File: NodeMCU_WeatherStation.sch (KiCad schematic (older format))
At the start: 3 parts, among them J4 Conn_01x04, J5 Conn_01x04, U1 BME280

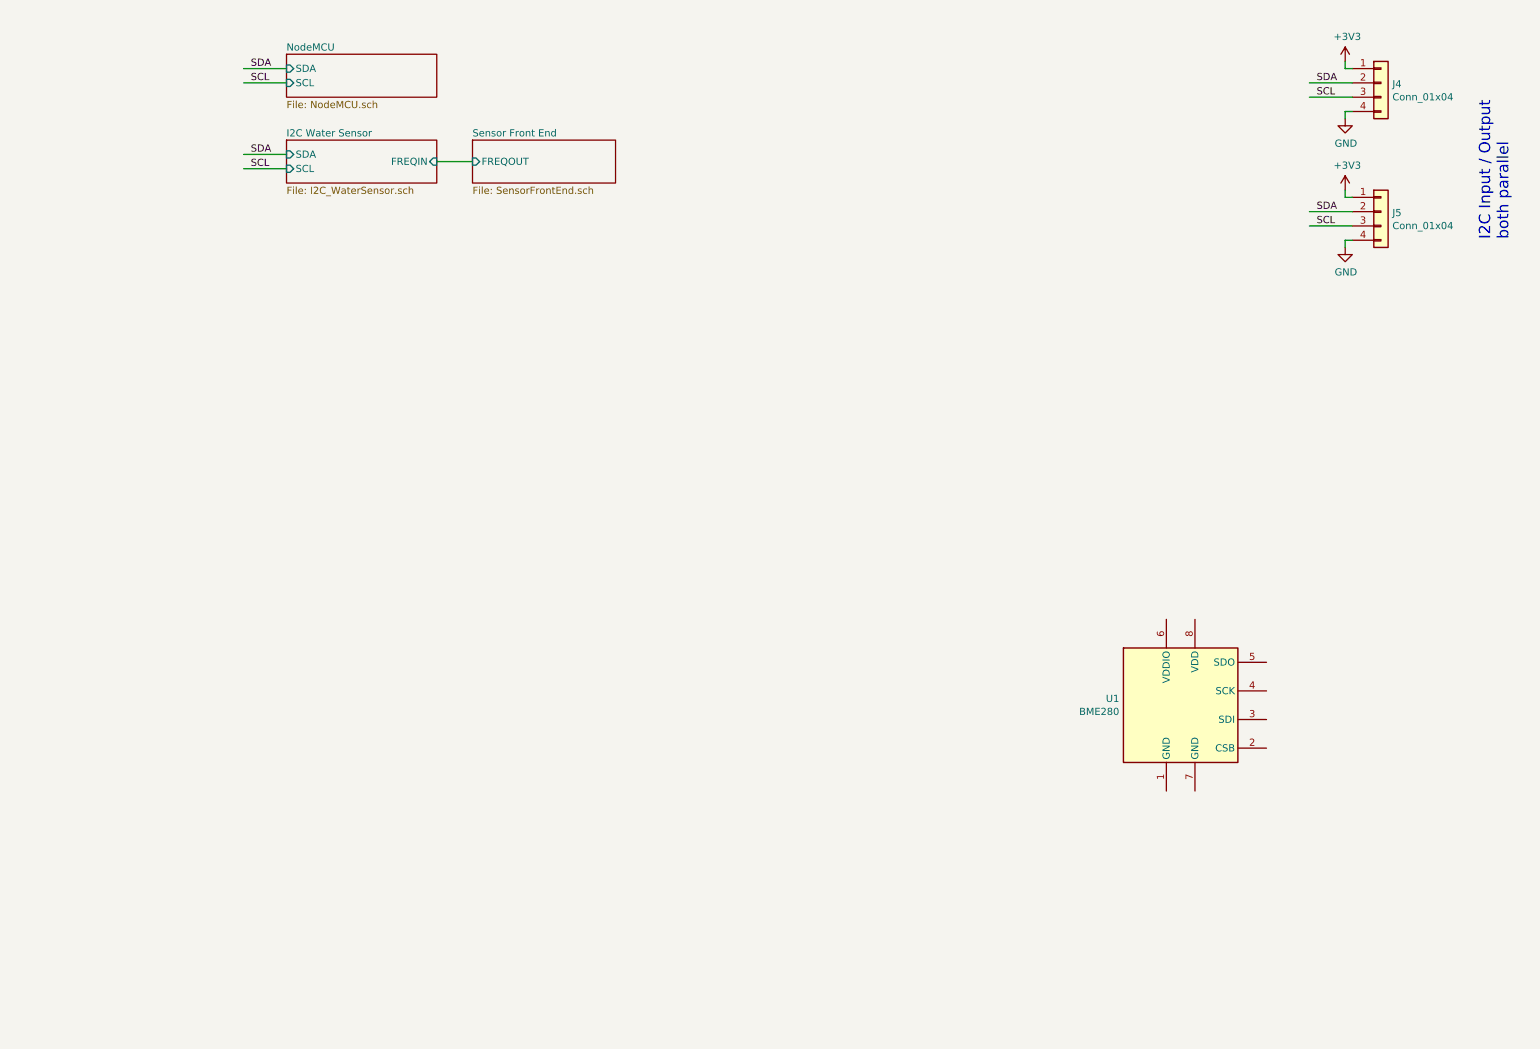
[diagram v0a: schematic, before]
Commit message: added 4-20mA input and PT100 readout
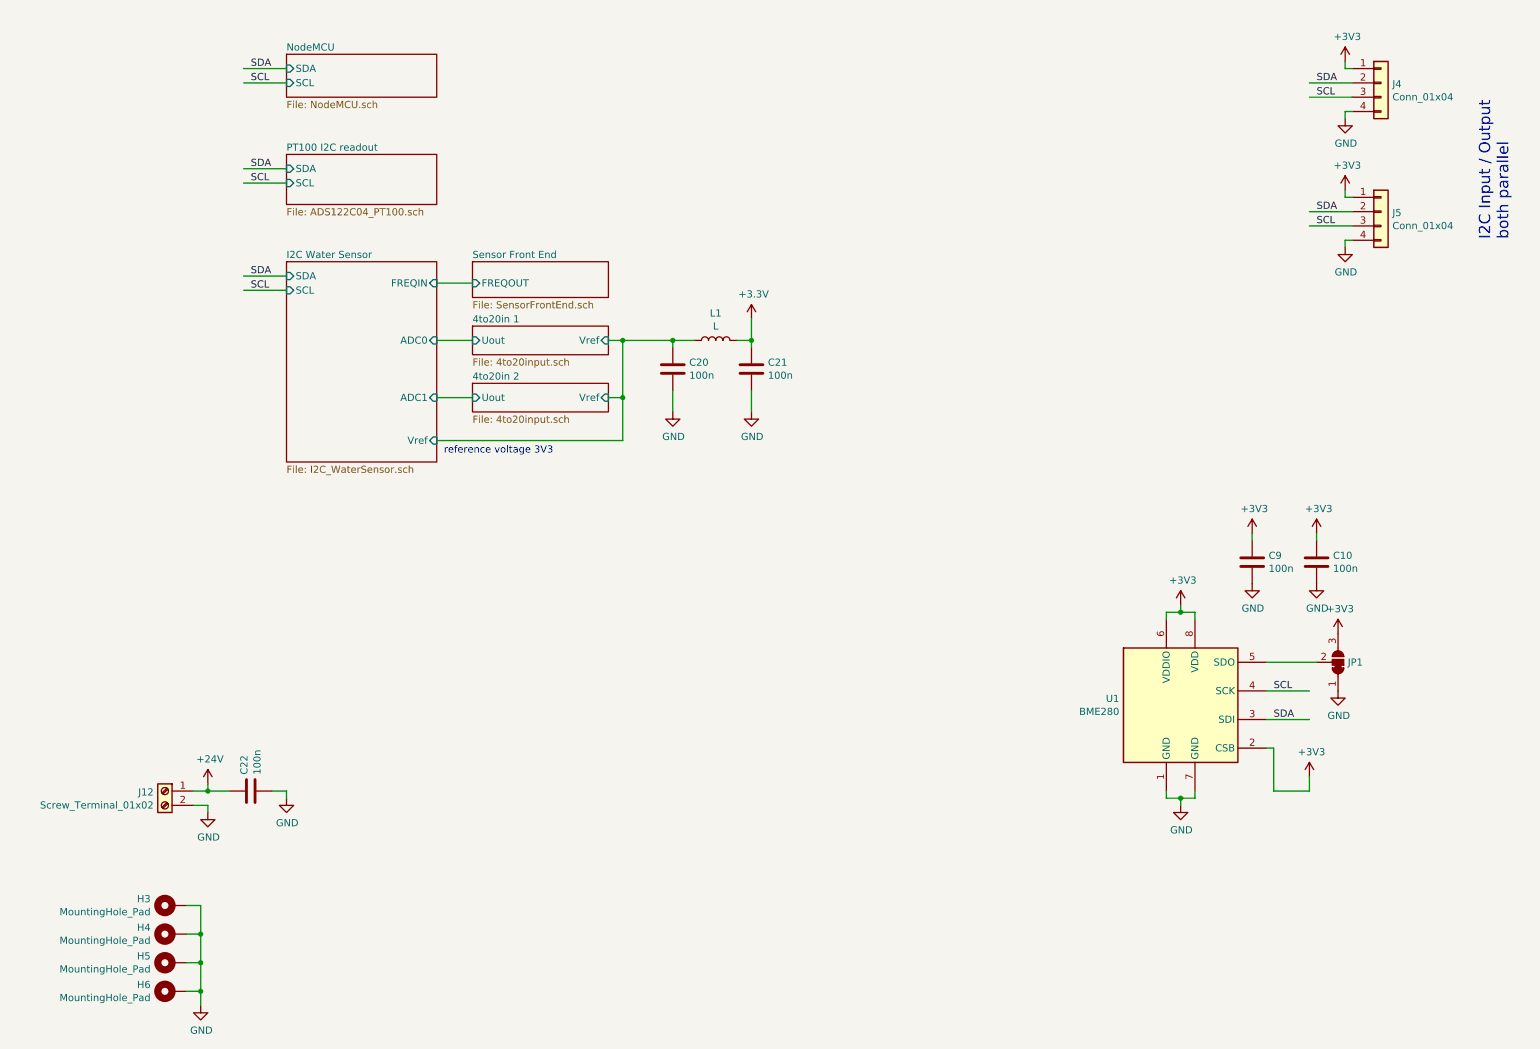
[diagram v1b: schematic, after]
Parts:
- added C10, C20, C21, C22, C9: 100n, Capacitor_SMD:C_0603_1608Metric, symbol Device:C
- added H3, H4, H5, H6: MountingHole_Pad, MountingHole:MountingHole_4.3mm_M4_Pad_Via, symbol Mechanical:MountingHole_Pad
- added J12: Screw_Terminal_01x02, TerminalBlock_MetzConnect:TerminalBlock_MetzConnect_Type055_RT01502HDWU_1x02_P5.00mm_Horizontal, symbol Connector:Screw_Terminal_01x02
- added JP1: SolderJumper_3_Bridged12, Jumper:SolderJumper-3_P1.3mm_Bridged12_Pad1.0x1.5mm, symbol Jumper:SolderJumper_3_Bridged12
- added L1: L, Inductor_SMD:L_0805_2012Metric, symbol Device:L
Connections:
- net labels added: +24V, +3.3V
- wire segments 17 -> 68
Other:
- note added: "reference voltage 3V3"

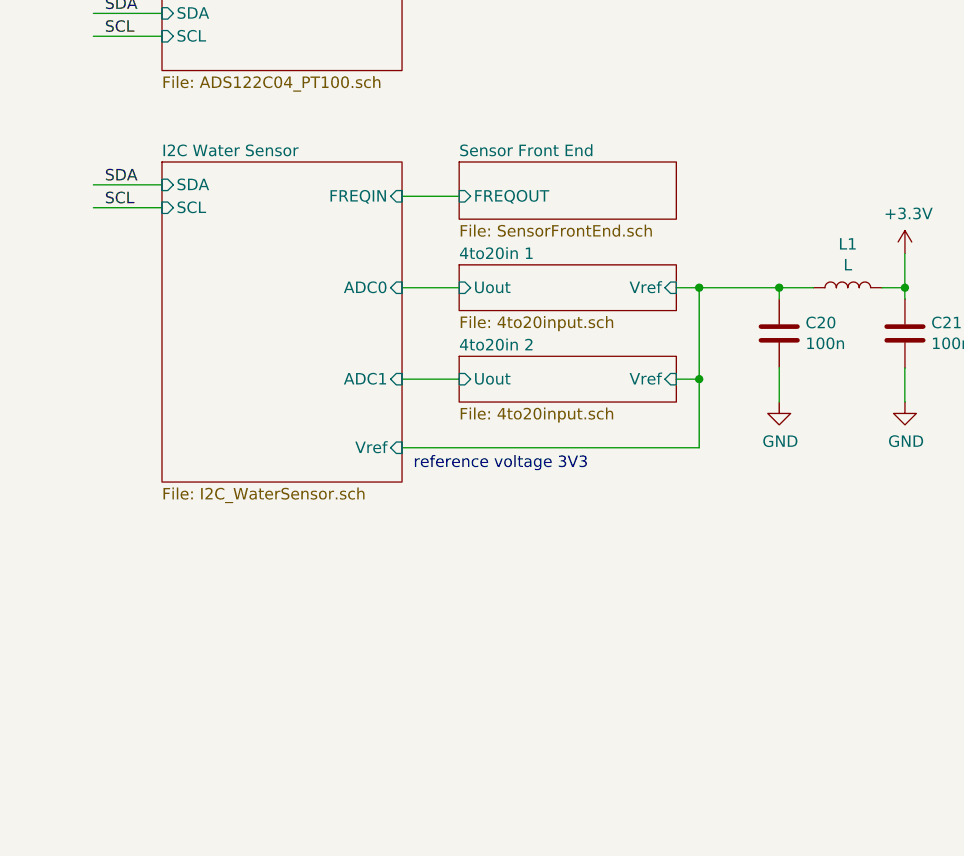
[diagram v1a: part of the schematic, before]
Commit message: added BPW34 for measurement of light intensity
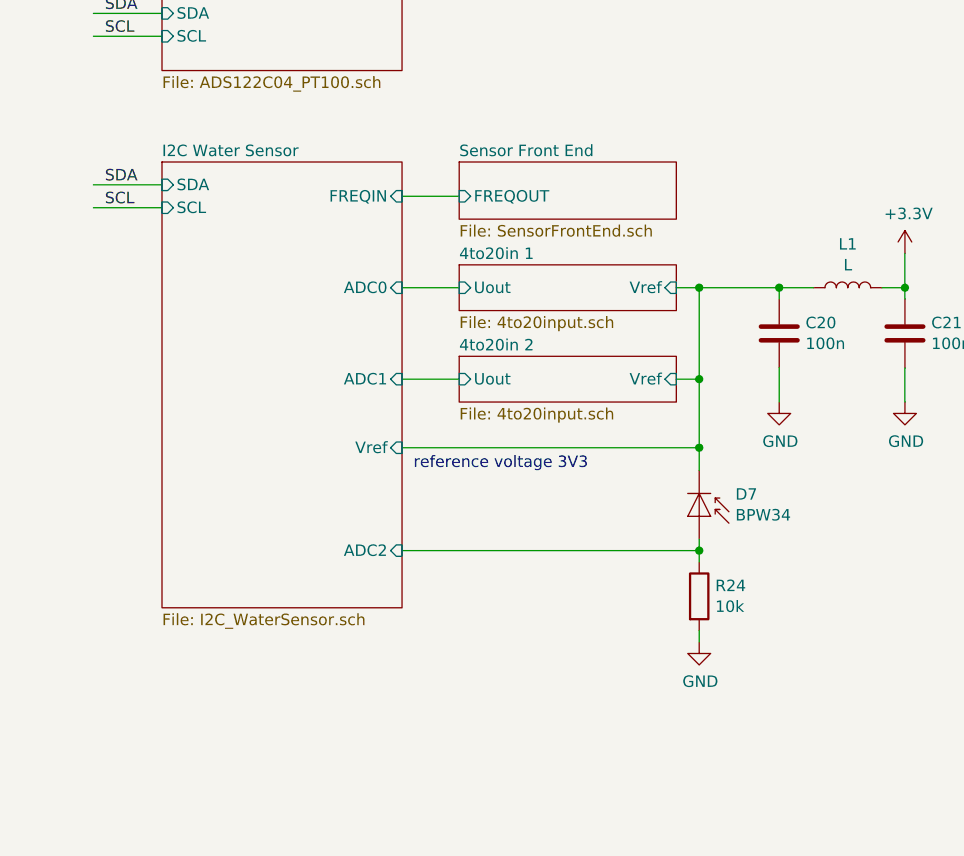
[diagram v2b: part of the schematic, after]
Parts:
- added D7: BPW34, OptoDevice:Osram_DIL2_4.3x4.65mm_P5.08mm, symbol Sensor_Optical:BPW34
- added R24: 10k, Resistor_SMD:R_0603_1608Metric, symbol Device:R
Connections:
- wire segments 68 -> 73
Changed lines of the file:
@@
 	1800 6100 1800 6150
 $Sheet
-S 2350 2300 1050 1400
+S 2350 2300 1050 1950
 U 5E788D14
 F0 "I2C Water Sensor" 50
@@
 F6 "ADC1" I R 3400 3250 50
 F7 "Vref" I R 3400 3550 50
+F8 "ADC2" I R 3400 4000 50
 $EndSheet
 Wire Wire Line
@@
 	2350 6000 2350 6050
 Connection ~ 1800 6000
+$Comp
+L Device:R R?
+U 1 1 5EDECD80
+P 4700 4200
+AR Path="/5E788D14/5EDECD80" Ref="R?"  Part="1"
+AR Path="/5EDECD80" Ref="R24"  Part="1"
+F 0 "R24" H 4770 4246 50  0000 L CNN
+F 1 "10k" H 4770 4155 50  0000 L CNN
+F 2 "Resistor_SMD:R_0603_1608Metric" V 4630 4200 50  0001 C CNN
+F 3 "~" H 4700 4200 50  0001 C CNN
+	1    4700 4200
+	1    0    0    -1
+$EndComp
+Wire Wire Line
+	4700 4050 4700 4000
+Wire Wire Line
+	4700 4350 4700 4400
+$Comp
+L power:GND #PWR?
+U 1 1 5EDEE714
+P 4700 4400
+AR Path="/5EE42DF1/5EDEE714" Ref="#PWR?"  Part="1"
+AR Path="/5EE46703/5EDEE714" Ref="#PWR?"  Part="1"
+AR Path="/5EDEE714" Ref="#PWR0107"  Part="1"
+F 0 "#PWR0107" H 4700 4150 50  0001 C CNN
+F 1 "GND" H 4705 4227 50  0000 C CNN
+F 2 "" H 4700 4400 50  0001 C CNN
+F 3 "" H 4700 4400 50  0001 C CNN
+	1    4700 4400
+	1    0    0    -1
+$EndComp
+Connection ~ 4700 4000
+Wire Wire Line
+	4700 4000 4700 3950
+Wire Wire Line
+	3400 4000 4700 4000
+$Comp
+L Sensor_Optical:BPW34 D7
+U 1 1 5EDE69A2
+P 4700 3850
+F 0 "D7" V 4604 4008 50  0000 L CNN
+F 1 "BPW34" V 4695 4008 50  0000 L CNN
+F 2 "OptoDevice:Osram_DIL2_4.3x4.65mm_P5.08mm" H 4700 4025 50  0001 C CNN
+F 3 "http://www.vishay.com/docs/81521/bpw34.pdf" H 4650 3850 50  0001 C CNN
+	1    4700 3850
+	0    1    1    0
+$EndComp
+Wire Wire Line
+	4700 3650 4700 3550
+Connection ~ 4700 3550
 $EndSCHEMATC

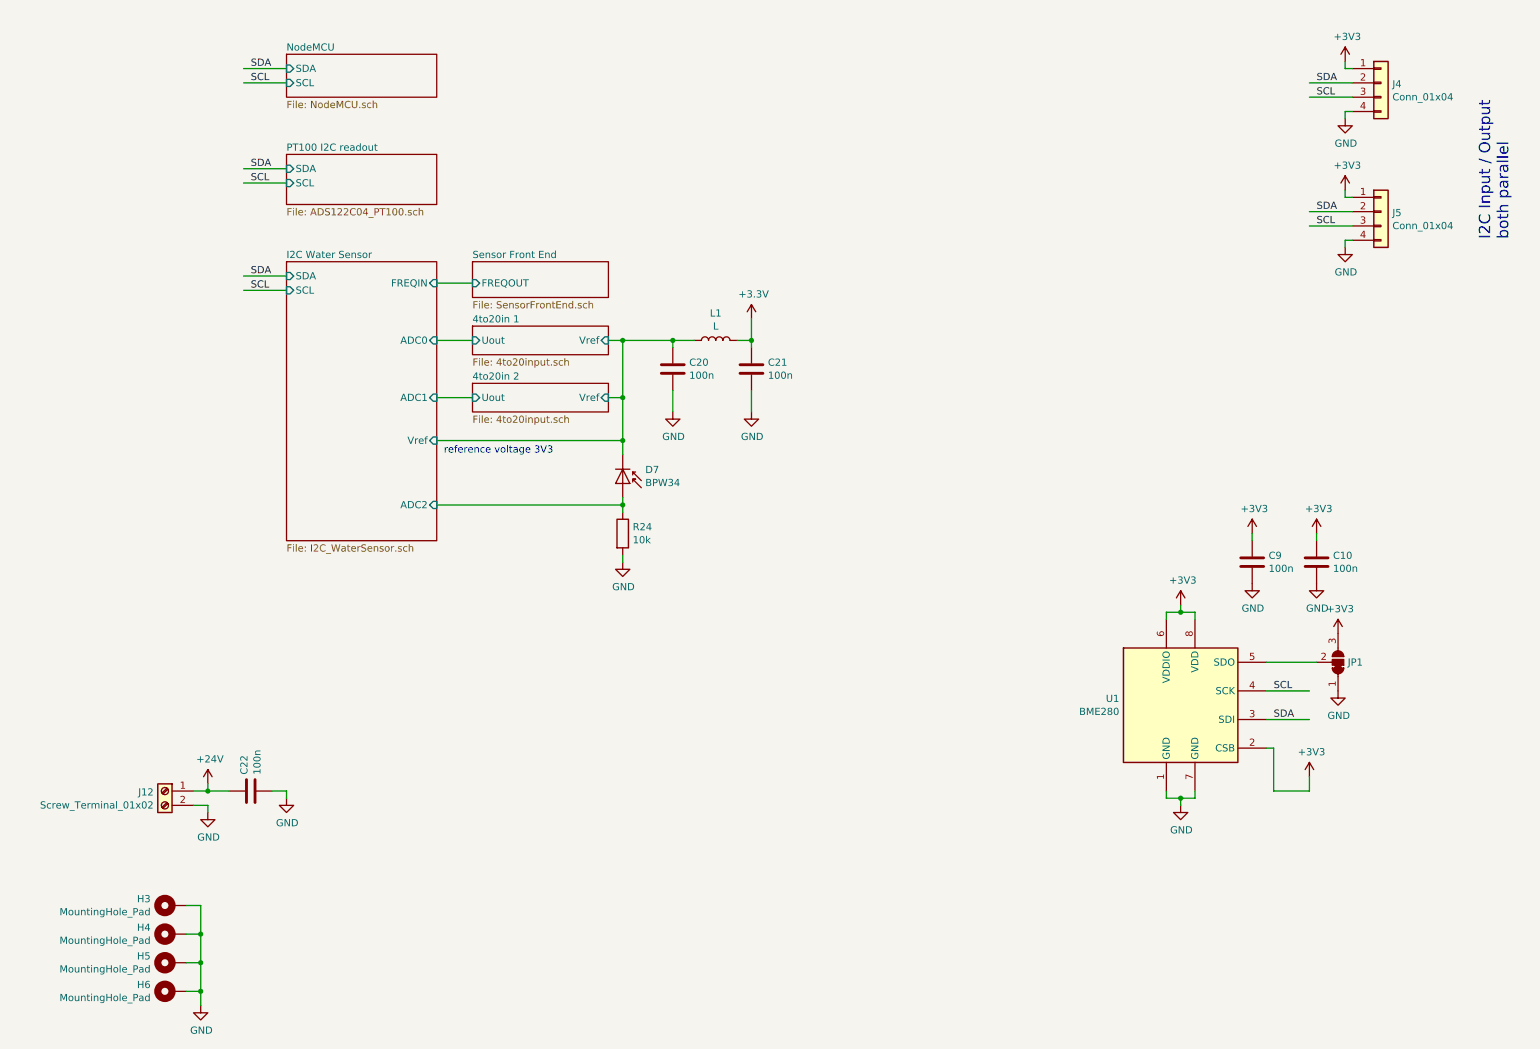
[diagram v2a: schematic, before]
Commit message: added digital output, 24V to 5V voltage regulator
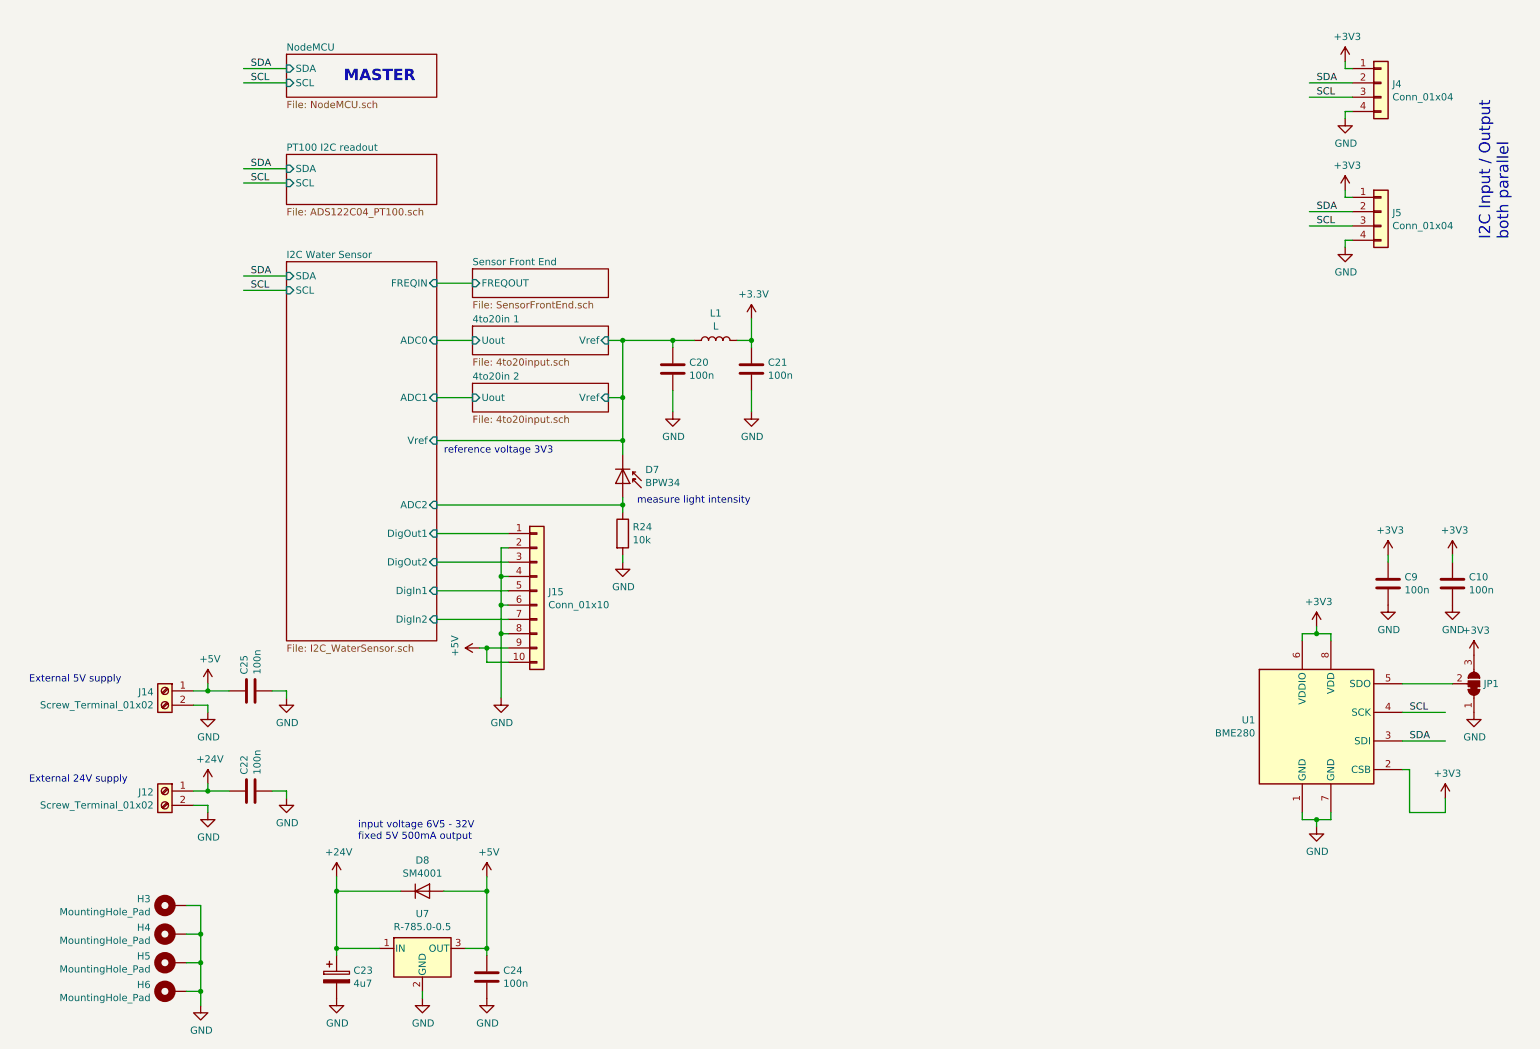
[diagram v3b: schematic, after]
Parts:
- added C23: 4u7, Capacitor_SMD:CP_Elec_10x10, symbol Device:CP
- added C24, C25: 100n, Capacitor_SMD:C_0603_1608Metric, symbol Device:C
- added D8: SM4001, Diode_SMD:D_MELF, symbol Diode:SM4001
- added J14: Screw_Terminal_01x02, TerminalBlock_MetzConnect:TerminalBlock_MetzConnect_Type055_RT01502HDWU_1x02_P5.00mm_Horizontal, symbol Connector:Screw_Terminal_01x02
- added J15: Conn_01x10, Connector_PinHeader_2.54mm:PinHeader_1x10_P2.54mm_Vertical, symbol Connector_Generic:Conn_01x10
- added U7: R-785.0-0.5, Converter_DCDC:Converter_DCDC_RECOM_R-78E-0.5_THT, symbol Regulator_Switching:R-785.0-0.5
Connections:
- net labels added: +5V
- wire segments 73 -> 107
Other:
- note added: "External 24V supply"
- note added: "External 5V supply"
- note added: "MASTER"
- note added: "input voltage 6V5 - 32V\nfixed 5V 500mA output"
- note added: "measure light intensity"
- moved on the sheet: C10, C9, JP1, U1
